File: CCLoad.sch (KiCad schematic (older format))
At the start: 32 parts

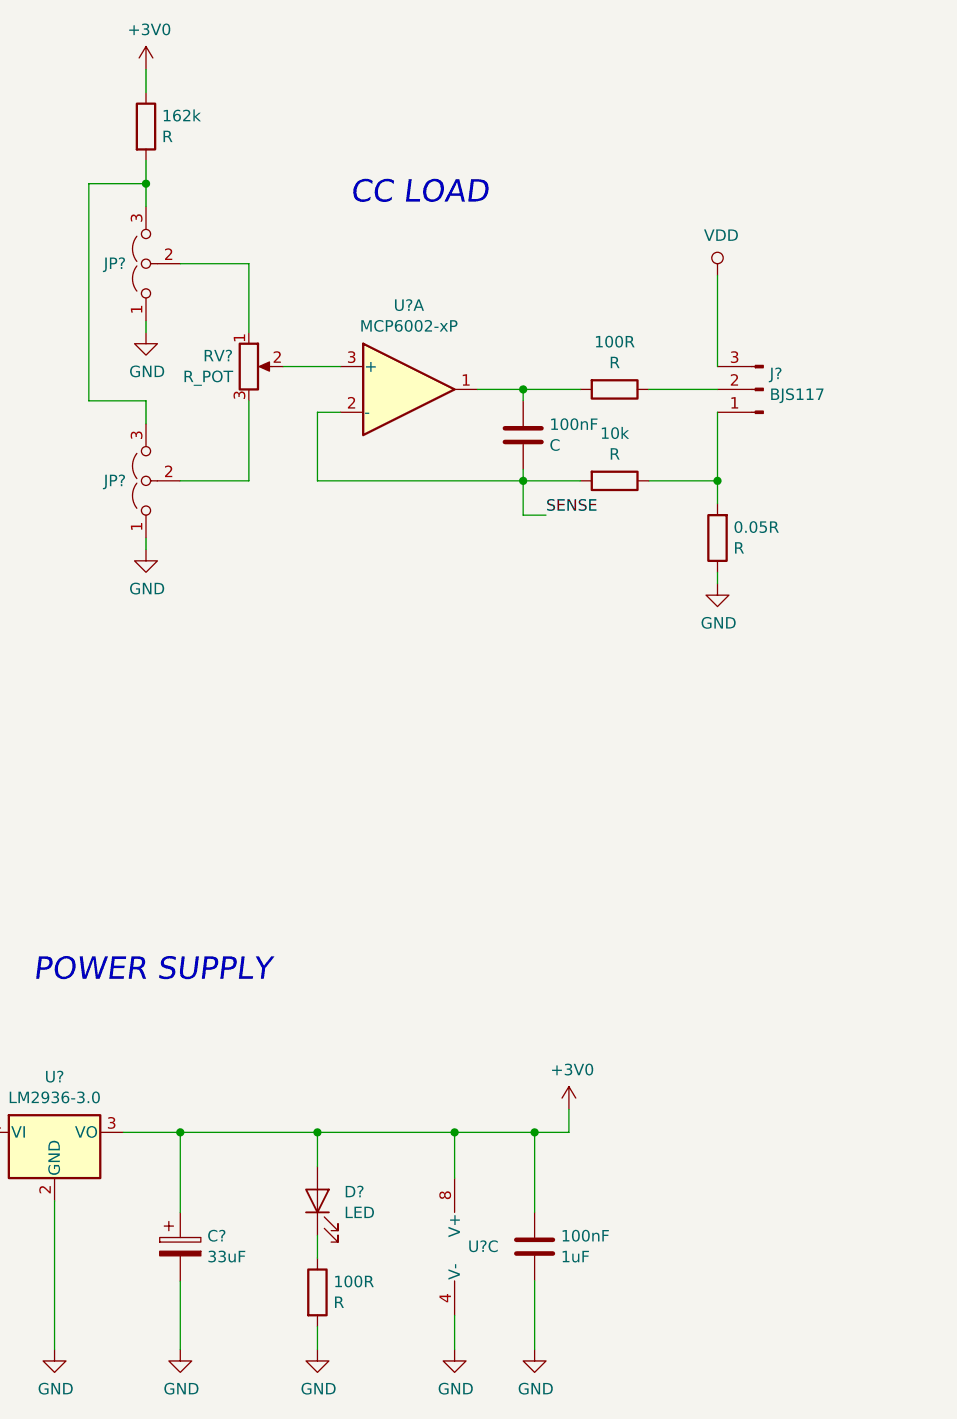
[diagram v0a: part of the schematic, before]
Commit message: fixes references
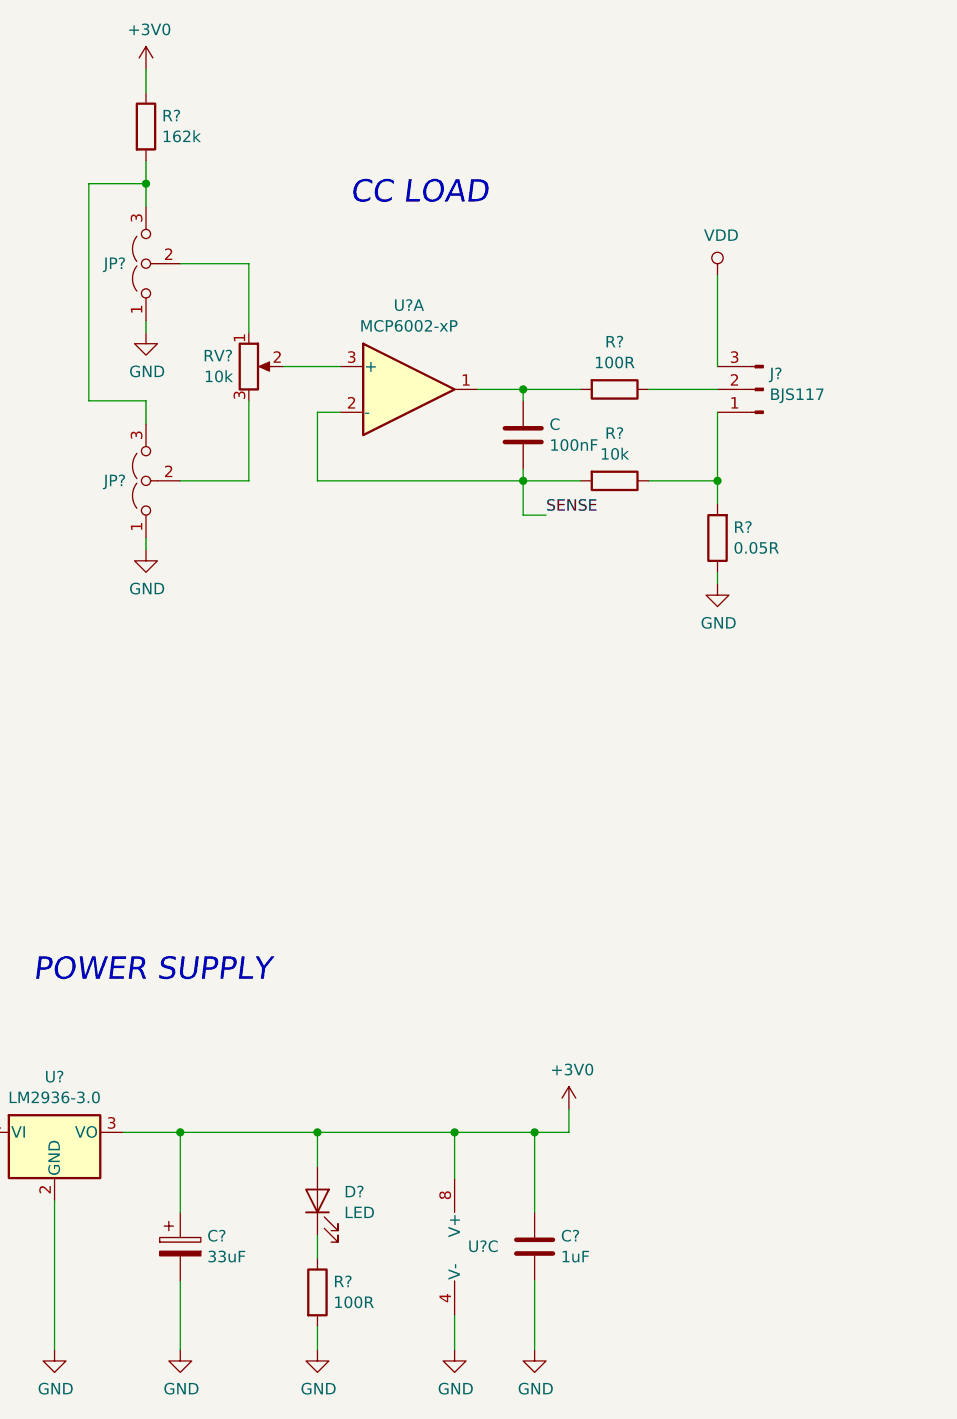
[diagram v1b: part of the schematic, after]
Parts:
- C: renamed from 100nF; value C -> 100nF
- R? (x2): renamed from 100R; value R -> 100R
- R?: renamed from 162k; value R -> 162k
- R?: renamed from 10k; value R -> 10k
- R?: renamed from 0.05R; value R -> 0.05R
- RV?: value R_POT -> 10k
- renumbered 100nF to C?
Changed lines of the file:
@@
 $EndComp
 $Comp
-L Device:R 100R
+L Device:R R?
 U 1 1 5DB82215
 P 4400 6500
-F 0 "100R" H 4470 6546 50  0000 L CNN
-F 1 "R" H 4470 6455 50  0000 L CNN
+F 0 "R?" H 4470 6546 50  0000 L CNN
+F 1 "100R" H 4470 6455 50  0000 L CNN
 F 2 "" V 4330 6500 50  0001 C CNN
 F 3 "~" H 4400 6500 50  0001 C CNN
@@
 $EndComp
 $Comp
-L Device:R 162k
+L Device:R R?
 U 1 1 5DBB446E
 P 3650 1400
-F 0 "162k" H 3720 1446 50  0000 L CNN
-F 1 "R" H 3720 1355 50  0000 L CNN
+F 0 "R?" H 3720 1446 50  0000 L CNN
+F 1 "162k" H 3720 1355 50  0000 L CNN
 F 2 "" V 3580 1400 50  0001 C CNN
 F 3 "~" H 3650 1400 50  0001 C CNN
@@
 P 4100 2450
 F 0 "RV?" H 4031 2496 50  0000 R CNN
-F 1 "R_POT" H 4031 2405 50  0000 R CNN
+F 1 "10k" H 4031 2405 50  0000 R CNN
 F 2 "" H 4100 2450 50  0001 C CNN
 F 3 "~" H 4100 2450 50  0001 C CNN
@@
 	4500 2450 4250 2450
 $Comp
-L Device:C 100nF
+L Device:C C?
 U 1 1 5DBCDC13
 P 5350 6300
-F 0 "100nF" H 5465 6346 50  0000 L CNN
+F 0 "C?" H 5465 6346 50  0000 L CNN
 F 1 "1uF" H 5465 6255 50  0000 L CNN
 F 2 "" H 5388 6150 50  0001 C CNN
@@
 	4400 2650 4400 2950
 $Comp
-L Device:C 100nF
+L Device:C C
 U 1 1 5DBD1A4D
 P 5300 2750
-F 0 "100nF" H 5415 2796 50  0000 L CNN
-F 1 "C" H 5415 2705 50  0000 L CNN
+F 0 "C" H 5415 2796 50  0000 L CNN
+F 1 "100nF" H 5415 2705 50  0000 L CNN
 F 2 "" H 5338 2600 50  0001 C CNN
 F 3 "~" H 5300 2750 50  0001 C CNN
@@
 	5300 2550 5100 2550
 $Comp
-L Device:R 100R
+L Device:R R?
 U 1 1 5DBD3A1C
 P 5700 2550
-F 0 "100R" V 5493 2550 50  0000 C CNN
-F 1 "R" V 5584 2550 50  0000 C CNN
+F 0 "R?" V 5493 2550 50  0000 C CNN
+F 1 "100R" V 5584 2550 50  0000 C CNN
 F 2 "" V 5630 2550 50  0001 C CNN
 F 3 "~" H 5700 2550 50  0001 C CNN
@@
 Connection ~ 5300 2550
 $Comp
-L Device:R 10k
+L Device:R R?
 U 1 1 5DBD5384
 P 5700 2950
-F 0 "10k" V 5493 2950 50  0000 C CNN
-F 1 "R" V 5584 2950 50  0000 C CNN
+F 0 "R?" V 5493 2950 50  0000 C CNN
+F 1 "10k" V 5584 2950 50  0000 C CNN
 F 2 "" V 5630 2950 50  0001 C CNN
 F 3 "~" H 5700 2950 50  0001 C CNN
@@
 Connection ~ 5300 2950
 $Comp
-L Device:R 0.05R
+L Device:R R?
 U 1 1 5DBD6B72
 P 6150 3200
-F 0 "0.05R" H 6080 3154 50  0000 R CNN
-F 1 "R" H 6080 3245 50  0000 R CNN
+F 0 "R?" H 6080 3154 50  0000 R CNN
+F 1 "0.05R" H 6080 3245 50  0000 R CNN
 F 2 "" V 6080 3200 50  0001 C CNN
 F 3 "~" H 6150 3200 50  0001 C CNN

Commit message: finished board, generated output files
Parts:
- removed J?: MOLEX, symbol Connector:Conn_01x02_Male
- removed SW?: SW_SPDT_MSM, symbol Switch:SW_SPDT_MSM
- added BT101: Battery_Cell, Battery:BatteryHolder_Keystone_1060_1x2032, symbol Device:Battery_Cell
- added C102: 10uF, Capacitor_Tantalum_SMD:CP_EIA-3216-12_Kemet-S_Pad1.58x1.35mm_HandSolder, symbol Device:CP
- added JP101: Jumper_2_Bridged, Jumper:SolderJumper-2_P1.3mm_Bridged_RoundedPad1.0x1.5mm, symbol Jumper:Jumper_2_Bridged
- added JP104: Jumper_2_Open, Jumper:SolderJumper-2_P1.3mm_Open_RoundedPad1.0x1.5mm, symbol Jumper:Jumper_2_Open
- added R102: 330R, Resistor_SMD:R_0805_2012Metric_Pad1.15x1.40mm_HandSolder, symbol Device:R
- added R103: 82k, Resistor_SMD:R_0805_2012Metric_Pad1.15x1.40mm_HandSolder, symbol Device:R
- added R108: 0.1R, Resistor_SMD:R_2512_6332Metric_Pad1.52x3.35mm_HandSolder, symbol Device:R
- added SW101: SW_DP3T, CCLoad:SW_DP3T_ALPS_SSSS223600, symbol CCLoad:SW_DP3T
- added U102: CJ431, Package_TO_SOT_SMD:SOT-23, symbol Reference_Voltage:TL432DBZ
- C101, C104: renamed from C?; footprint (none) -> Capacitor_SMD:C_0805_2012Metric_Pad1.15x1.40mm_HandSolder
- C103: renamed from C?; value 33uF -> 10uF; footprint (none) -> Capacitor_Tantalum_SMD:CP_EIA-3216-12_Kemet-S_Pad1.58x1.35mm_HandSolder; LCSC (none) -> C7171
- C105: renamed from C; footprint (none) -> Capacitor_SMD:C_0805_2012Metric_Pad1.15x1.40mm_HandSolder
- D101: renamed from D?; footprint (none) -> LED_SMD:LED_0805_2012Metric_Pad1.15x1.40mm_HandSolder
- H101: renamed from H1; footprint MountingHole:MountingHole_3.7mm_Pad_Via -> MountingHole:MountingHole_3.7mm_Pad
- H102: renamed from H2; footprint MountingHole:MountingHole_3.7mm_Pad_Via -> MountingHole:MountingHole_3.7mm_Pad
- H103: renamed from H3; footprint MountingHole:MountingHole_3.7mm_Pad_Via -> MountingHole:MountingHole_3.7mm_Pad
- H104: renamed from H4; footprint MountingHole:MountingHole_3.7mm_Pad_Via -> MountingHole:MountingHole_3.7mm_Pad
- J101, J102: renamed from J?; footprint (none) -> CCLoad:Binding_Post_Caltest_CT2234
- J103, J106: renamed from J?; footprint (none) -> Connector_PinHeader_2.54mm:PinHeader_1x02_P2.54mm_Vertical
- J104: renamed from J?; value BJS117 -> BTS117; footprint (none) -> CCLoad:BTS117_outboard
- J105: renamed from J?; footprint (none) -> Connector_Molex:Molex_KK-254_AE-6410-02A_1x02_P2.54mm_Vertical
- JP102, JP103: renamed from JP?; footprint (none) -> Jumper:SolderJumper-3_P1.3mm_Bridged12_RoundedPad1.0x1.5mm
- R101, R104, R107, R109, R110: renamed from R?; footprint (none) -> Resistor_SMD:R_0805_2012Metric_Pad1.15x1.40mm_HandSolder
- R105: renamed from R?; value 10k -> 0R; footprint (none) -> Resistor_SMD:R_0805_2012Metric_Pad1.15x1.40mm_HandSolder
- R106: renamed from R?; value 0.05R -> 0.1R; footprint (none) -> Resistor_SMD:R_2512_6332Metric_Pad1.52x3.35mm_HandSolder; LCSC (none) -> C63324
- RV101: renamed from RV?; footprint (none) -> Potentiometer_THT:Potentiometer_Alps_RK09K_Single_Vertical; LCSC (none) -> C361173; PN (none) -> RK09D1130C2P
- RV102: renamed from RV?; footprint (none) -> Potentiometer_SMD:Potentiometer_Bourns_3314J_Vertical; LCSC (none) -> C124640
- U101: renamed from U?; value LM2936-3.0 -> HT7533-1 (3V3); footprint (none) -> Package_TO_SOT_SMD:SOT-89-3_Handsoldering; LCSC (none) -> C14289
- U103: renamed from U?; footprint (none) -> Package_SO:SOIC-8_3.9x4.9mm_P1.27mm
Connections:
- net BATTERY+: now also BT101.1 (+), SW101.4 (8), SW101.8
- net GND: now also JP102.3 (B), JP103.3 (B), BT101.2 (-), C102.2, R108.1, SW101.2 (6), U102.3 (A); no longer JP102.1 (A), JP103.1 (A)
- net VDD: now also C101.1, U101.1 (VI)
- net at J104.1 (Pin_1), R105.1, R106.2: now also R108.2
- net +3V0: no longer names the net of C103.1, C104.1, U103.8 (V+)
- net +3V0: now also R102.1, SW101.3 (7); no longer D101.2 (A), R101.1, U101.3 (VO)
- new net: C102.1, SW101.1 (5), U101.3 (VO)
- new net: D101.2 (A), SW101.7
- new net: JP101.2 (B), R101.2
- new net: JP101.1 (A), JP102.1 (A), JP103.1 (A), JP104.1 (A)
- new net: JP104.2 (B), R103.2
- new net +2V5: R101.1, R102.2, R103.1, U102.1 (REF), U102.2 (K)
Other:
- note added: "Imax = 3A"
- note added: "Imax = 5.5A"
- note added: "Keep C close to opamp pins"
- moved on the sheet: C101, C103, C104, C105, D101, J101, J102, J103, J104, JP102, JP103, R101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
